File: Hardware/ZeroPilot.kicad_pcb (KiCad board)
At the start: 4 copper layers, 100 x 70 mm, 246 parts, among them J1 Conn_01x03, J10 Conn_01x03, J11 Conn_01x03, J12 Conn_01x03, J13 SPOX-2, J14 Micro_SD_Card, J15 USB_MICRO_B, J16 SPOX-3, J17 SPOX-3, J18 SPOX-4, J19 SPOX-2, J2 Conn_01x03, J22 SPOX-4, J23 SPOX-4, J24 SPOX-6, J25 SPOX-6, J26 SPOX-6, J28 SPOX-6, J29 SPOX-6, J3 Conn_01x03, J30 SPOX-6, J4 Conn_01x03, J5 Conn_01x03, J6 Conn_01x03, J7 Conn_01x03, J8 Conn_01x03, J9 Conn_01x03, Q1 Q_PMOS_DGS, Q2 Q_NMOS_GSD, U1 TPS54308, U10 STM32F030RCT6, U11 M24C64-WDW6TP, U12 ICM-20602, U13 MS5637-02BA03, U14 FT4232H, U2 TPS54308DDCT, U3 NC7S04P5X, U4 TPS22810DRV, U5 TPS22810DRV, U6 TPS22810DRV, U7 TPS22810DRV, U8 MCP1826S-3302E/DB, U9 STM32F765ZGT6, Y1 32.768kHz, Y2 8MHz, Y3 32.768kHz, Y4 8MHz, Y5 Crystal_GND24

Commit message: Changed "Signals" in stackup text to "3.3V"
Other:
- board text added: "Stackup: L1 (Front): Main components and routing L2: Ground L3: 3.3V L4 (Back): USB, SD, more components and routing"
- board text removed: "Stackup: L1 (Front): Main components and routing L2: Ground L3: Signals L4 (Back): USB, SD, more components and routing"
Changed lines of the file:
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@@
     (links 565)
     (no_connects 6)
-    (area 42.734867 94.1 258.863289 174.200001)
+    (area 42.734867 94.1 293.291859 174.200001)
     (thickness 1.6)
     (drawings 5)
@@
       (net 76 /UHF_RX))
   )
-  (gr_text "Stackup:\nL1 (Front): Main components and routing\nL2: Ground\nL3: Signals\nL4 (Back): USB, SD, more components and routing" (at 176.149 120.802) (layer Dwgs.User)
+  (gr_text "Stackup:\nL1 (Front): Main components and routing\nL2: Ground\nL3: 3.3V\nL4 (Back): USB, SD, more components and routing" (at 176.149 120.802) (layer Dwgs.User)
     (effects (font (size 3 3) (thickness 0.3)) (justify left))
   )

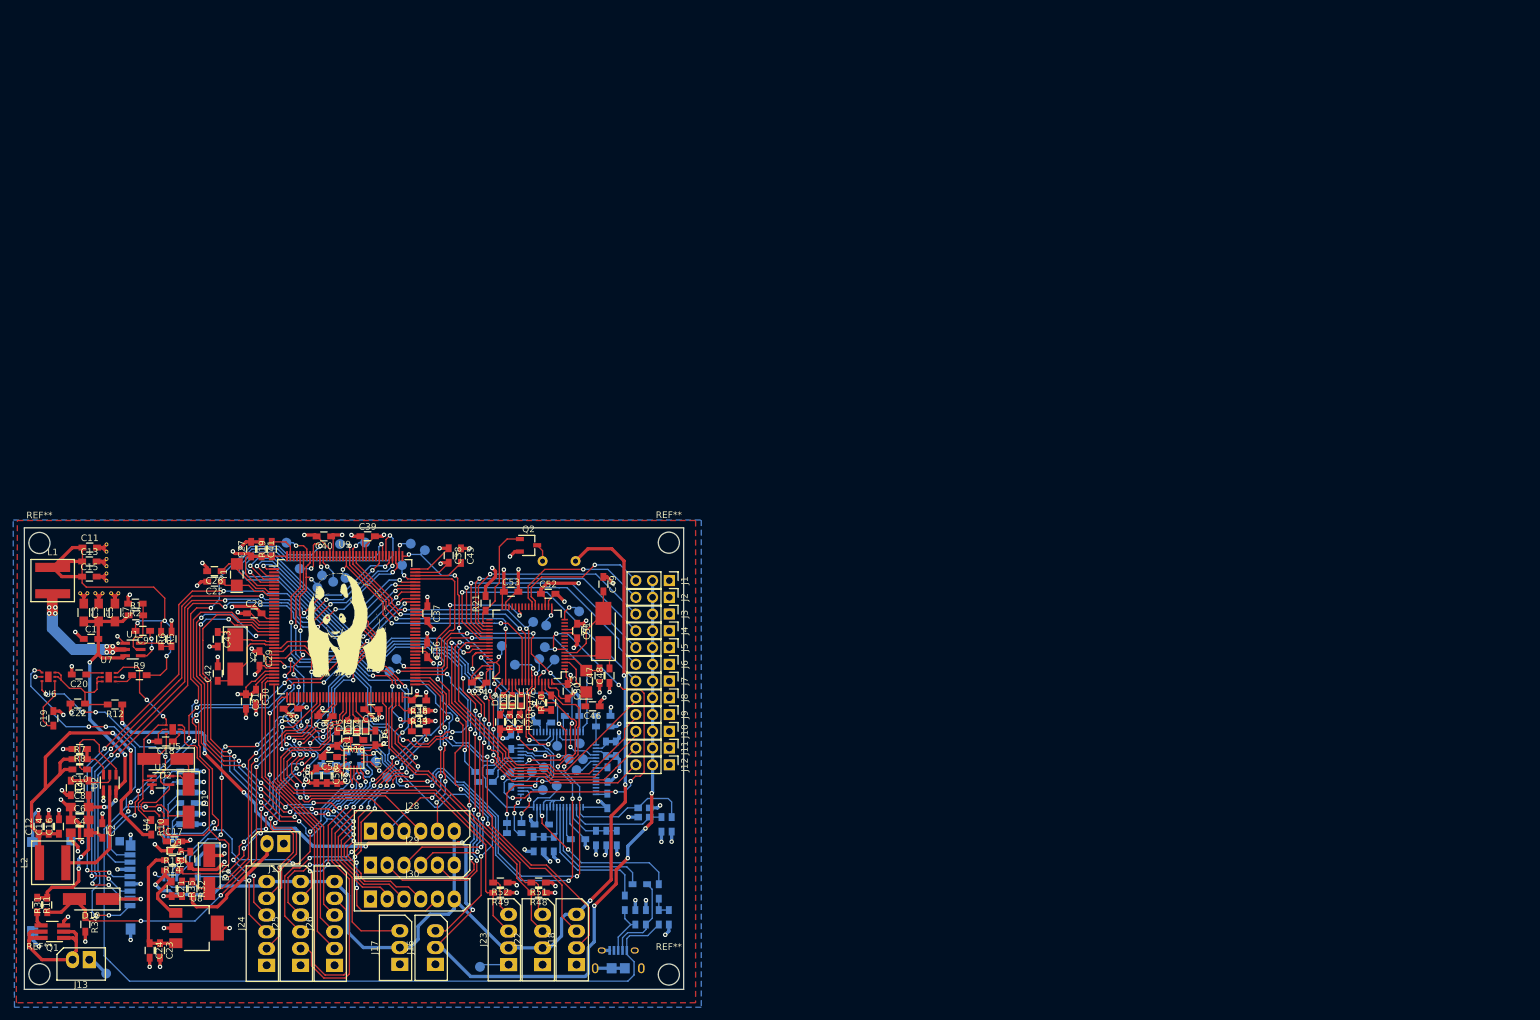
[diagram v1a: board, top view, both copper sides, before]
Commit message: Generated netlist and board outline
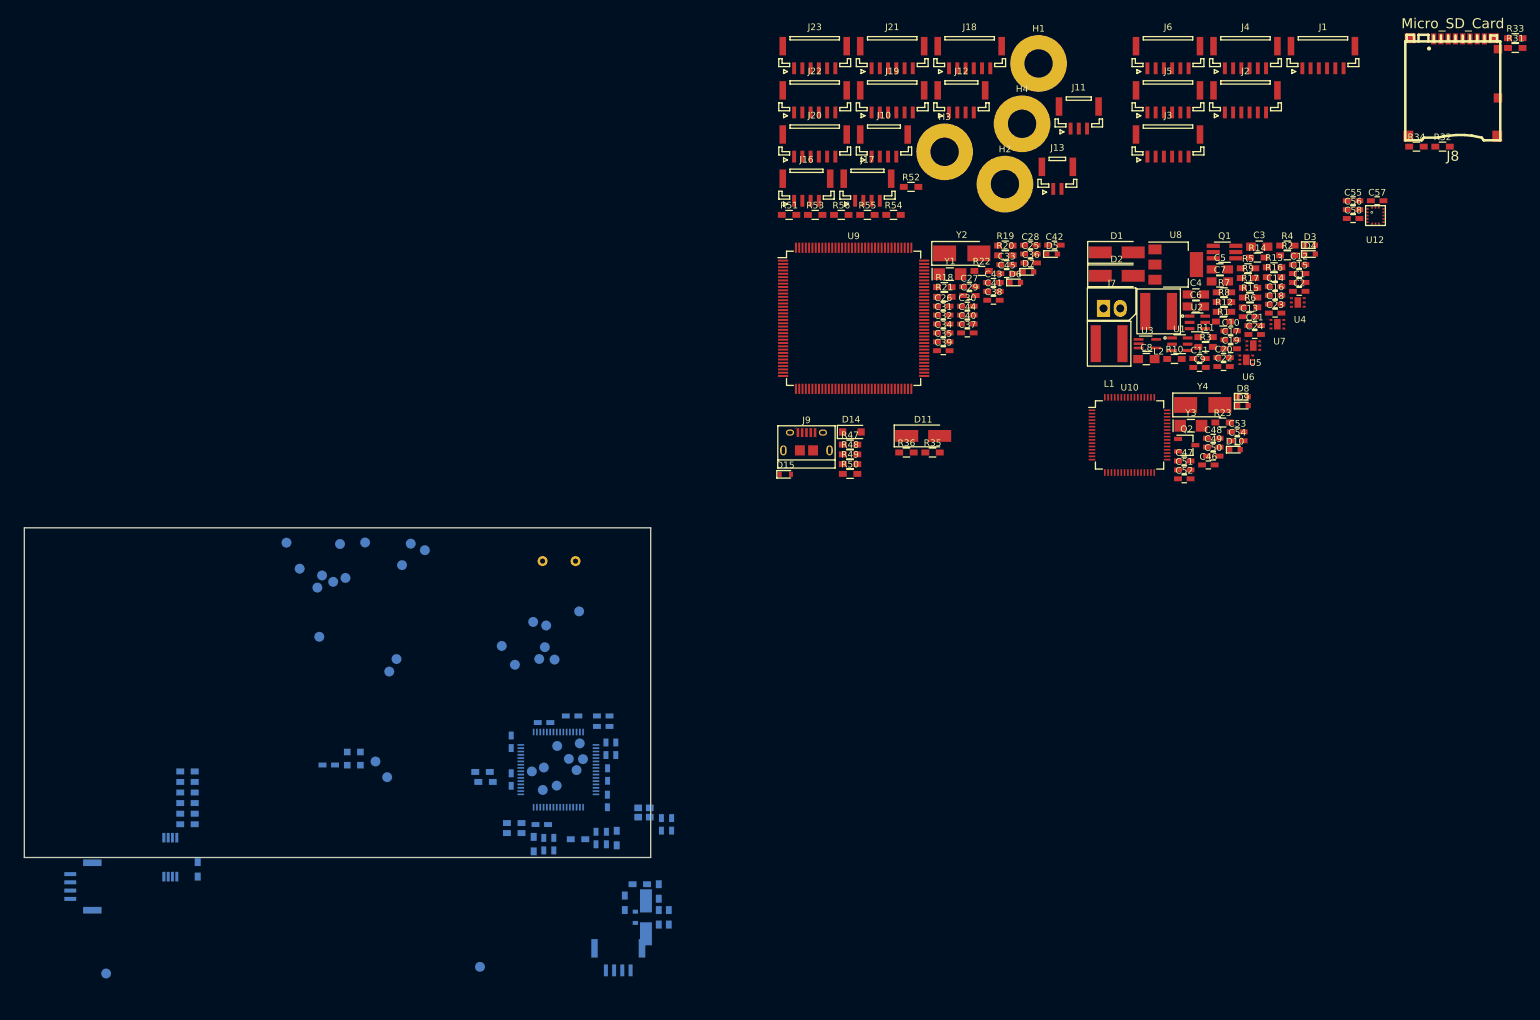
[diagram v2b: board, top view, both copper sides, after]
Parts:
- removed G***: LOGO, WARG:panda_small
- removed J24, J25, J26, J28, J29, J30: SPOX-6, Connectors_Molex:Molex_SPOX-5267_22-03-5065_06x2.54mm_Straight
- removed REF** (x12): via, WARG:via
- removed REF** (x4): MountingHole_3.2mm_M3, Mounting_Holes:MountingHole_3.2mm_M3
- added D14: D_Schottky, Diodes_SMD:D_SOD-123F, F.Cu at (175.5, 85.5)
- added D15: TVS, Diodes_SMD:D_0603, F.Cu at (165.4, 91.9)
- added H1: MountingHole_M4, Mounting_Holes:MountingHole_4.3mm_M4_Pad, F.Cu at (203.8, 29.6)
- added H2: MountingHole_M4, Mounting_Holes:MountingHole_4.3mm_M4_Pad, F.Cu at (198.7, 47.9)
- added H3: MountingHole_M4, Mounting_Holes:MountingHole_4.3mm_M4_Pad, F.Cu at (189.6, 43.0)
- added H4: MountingHole_M4, Mounting_Holes:MountingHole_4.3mm_M4_Pad, F.Cu at (201.3, 38.7)
- added J20: GH-6, Connectors_JST:JST_GH_BM06B-GHS-TBT_06x1.25mm_Straight, F.Cu at (169.9, 42.0)
- added J21: GH-6, Connectors_JST:JST_GH_BM06B-GHS-TBT_06x1.25mm_Straight, F.Cu at (181.6, 28.6)
- added R53: 10K, Resistors_SMD:R_0603_HandSoldering, F.Cu at (169.9, 52.5)
- added R54: 10K, Resistors_SMD:R_0603_HandSoldering, F.Cu at (181.8, 52.5)
- added R55: 10K, Resistors_SMD:R_0603_HandSoldering, F.Cu at (177.9, 52.5)
- added R56: 10K, Resistors_SMD:R_0603_HandSoldering, F.Cu at (173.9, 52.5)
- C1, C10, C11, C12, C13, C14, C15, C16, C17, C18, C19, C2, C20, C21, C22, C23, C24, C25, C26, C27, C28, C29, C30, C31, C32, C33, C34, C35, C36, C37, C38, C39, C40, C41, C42, C43, C44, C45, C46, C47, C48, C49, C50, C51, C52, C53, C54, C55, C57, C59, C60, C61, C62, C63, C64, C65, C66, C67, C68, C69, C70, C71, C72, C73, C74, C75, C76, C9: footprint Resistors_SMD:R_0603_HandSoldering -> Capacitors_SMD:C_0603_HandSoldering
- C3, C4, C5, C6, C7, C8: footprint Resistors_SMD:R_0805_HandSoldering -> Capacitors_SMD:C_0805_HandSoldering
- C56, C58: value 0.1uF -> 100nF; footprint Resistors_SMD:R_0603_HandSoldering -> Capacitors_SMD:C_0603_HandSoldering
- D1, D2: value S1B-13-F -> D
- D10: value D -> LED; footprint Diodes_SMD:D_SMA_Handsoldering -> LEDs:LED_0603
- D12: value TVS -> D; footprint Resistors_SMD:R_0603_HandSoldering -> Diodes_SMD:D_SMA_Handsoldering
- D13: footprint Resistors_SMD:R_0603_HandSoldering -> Diodes_SMD:D_0603
- D4: value LED -> PWR_LED
- J1, J2, J3, J4, J5, J6: value Conn_01x03 -> GH-6; footprint Pin_Headers:Pin_Header_Straight_1x03_Pitch2.54mm -> Connectors_JST:JST_GH_BM06B-GHS-TBT_06x1.25mm_Straight
- J10, J12: value Conn_01x03 -> GH-4; footprint Pin_Headers:Pin_Header_Straight_1x03_Pitch2.54mm -> Connectors_JST:JST_GH_BM04B-GHS-TBT_04x1.25mm_Straight
- J11: value Conn_01x03 -> GH-3; footprint Pin_Headers:Pin_Header_Straight_1x03_Pitch2.54mm -> Connectors_JST:JST_GH_BM03B-GHS-TBT_03x1.25mm_Straight
- J13: value SPOX-2 -> GH-2; footprint Connectors_Molex:Molex_SPOX-5267_22-03-5025_02x2.54mm_Straight -> Connectors_JST:JST_GH_BM02B-GHS-TBT_02x1.25mm_Straight
- J14: value Micro_SD_Card -> GH-4; footprint WARG:micro_sd -> Connectors_JST:JST_GH_BM04B-GHS-TBT_04x1.25mm_Straight
- J15: value USB_MICRO_B -> GH-4; footprint WARG:USB_Micro-B_10118194-0001LF -> Connectors_JST:JST_GH_BM04B-GHS-TBT_04x1.25mm_Straight
- J16, J17: value SPOX-3 -> GH-4; footprint Connectors_Molex:Molex_SPOX-5267_22-03-5035_03x2.54mm_Straight -> Connectors_JST:JST_GH_BM04B-GHS-TBT_04x1.25mm_Straight
- J18, J22, J23: value SPOX-4 -> GH-6; footprint Connectors_Molex:Molex_SPOX-5267_22-03-5045_04x2.54mm_Straight -> Connectors_JST:JST_GH_BM06B-GHS-TBT_06x1.25mm_Straight
- J19: value SPOX-2 -> GH-6; footprint Connectors_Molex:Molex_SPOX-5267_22-03-5025_02x2.54mm_Straight -> Connectors_JST:JST_GH_BM06B-GHS-TBT_06x1.25mm_Straight
- J7: value Conn_01x03 -> SPOX-2; footprint Pin_Headers:Pin_Header_Straight_1x03_Pitch2.54mm -> Connectors_Molex:Molex_SPOX-5267_22-03-5025_02x2.54mm_Straight
- J8: value Conn_01x03 -> Micro_SD_Card; footprint Pin_Headers:Pin_Header_Straight_1x03_Pitch2.54mm -> WARG:micro_sd
- J9: value Conn_01x03 -> USB_MICRO_B; footprint Pin_Headers:Pin_Header_Straight_1x03_Pitch2.54mm -> WARG:USB_Micro-B_10118194-0001LF
- L3, L4: footprint Resistors_SMD:R_0603_HandSoldering -> Inductors_SMD:L_0603_HandSoldering
- R1: value 210k -> 210K
- R19, R26: value 0 -> 100
- R2: value 43.2k -> 43.2K
- R21: value 100K -> 10K
- R22: value 100 -> 0
- R24: value 0 -> 100K
- R25: value 10K -> 100
- R3: value 226k -> 226K
- R30, R48, R49: value 10K -> 0
- R31: value 150K -> 10K
- R32: value 150K -> 0
- R33: value 11K -> 10K
- R34: value 22K -> 10K
- R35, R36: value 22K -> 150K
- R37: value 4.7k -> 11K
- R38: value 10k -> 22K
- R39: value 12k -> 22K
- R4: value 56k -> 56K
- R40: value 10R -> 22K
- R41: value 10R -> 4.7K
- R42: value 1k -> 10K
- R43: value 220R -> 12K
- R44, R45: value 0R -> 10
- R46: value 220R -> 1K
- R47, R50: value 10K -> 220
- R5, R7: value 100k -> 100K
- R6: value 11k -> 11K
- R8: value 13.7k -> 13.7K
- TP10: value NRSTS_TST -> GND_TST
- TP11: value SWIOS_TST -> TXP_TST
- TP12: value SCLKS_TST -> RXP_TST
- TP13: value NRSTP_TST -> NRSTS_TST
- TP14: value SWIOP_TST -> SWIOS_TST
- TP15: value SCLKP_TST -> SCLKS_TST
- TP16: value GND_TST -> NRSTP_TST
- TP17: value TDO1_TST -> SWIOP_TST
- TP18: value TMS1_TST -> SCLKP_TST
- TP19: value TEST -> GND_TST
- TP20: value TDO2_TST -> TDO1_TST
- TP21: value TMS2_TST -> TMS1_TST
- TP22: value TEST -> TDO2_TST
- TP23: value UART1_RTS_TST -> TMS2_TST
- TP24: value UART1_CTS_TST -> UART1_RTS_TST
- TP25: value UART2_RTS_TST -> UART1_CTS_TST
- TP26: value UART2_CTS_TST -> UART2_RTS_TST
- TP27: value TEST -> UART2_CTS_TST
- TP5: value TXS_TST -> TEST
- TP6: value RXS_TST -> TEST
- TP7: value GND_TST -> TEST
- TP8: value TXP_TST -> TXS_TST
- TP9: value RXP_TST -> RXS_TST
- moved R31 257.8 mm to (276.1, 27.2), turned to 0 degrees
- moved R34 233.8 mm to (261.1, 42.2), turned to 0 degrees
- moved R32 220.5 mm to (265.1, 42.2), turned to 0 degrees
- moved C12 209.3 mm to (243.3, 60.1), turned to 0 degrees
- moved Q1 205.5 mm to (232.0, 58.2), turned to 0 degrees
- moved C14 203.2 mm to (239.7, 63.4), turned to 0 degrees
- moved R4 202.0 mm to (241.6, 57.2), turned to 0 degrees
- moved C16 201.3 mm to (239.7, 64.7), turned to 0 degrees
- moved C2 199.1 mm to (243.4, 64.1), turned to 0 degrees
- moved R11 197.0 mm to (229.2, 71.1), turned to 0 degrees
- moved R33 196.7 mm to (276.1, 25.7)
- moved D3 195.0 mm to (245.0, 57.1)
- moved C23 194.8 mm to (239.7, 67.4), turned to 0 degrees
- moved C24 191.9 mm to (236.6, 70.7), turned to 0 degrees
- moved C1 191.0 mm to (243.4, 62.8)
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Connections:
- C10 pad 2: /POWER/INT_BUCK -> /POWER/INT_SW
- C9 pad 2: /POWER/EXT_BUCK -> /POWER/EXT_SW
- D10 pad 1: /3V3 -> Net-(D10-Pad1)
- D10 pad 2: /VBATT_ADC -> Net-(D10-Pad2)
- D11 pad 2: /EXT_BATT_ADC -> /VBATT_ADC
- D12 pad 1: Net-(D12-Pad1) -> /3V3
- D12 pad 2: GND -> /V_ISENSE_ADC
- D4 pad 1: Net-(D4-Pad1) -> GND
- J1 pad 1: GND -> /6V_EXT
- J10 pad 2: /6V_EXT -> /RSSI
- J10 pad 3: /PWM 1-12/PWM10 -> /PPM
- J11 pad 2: /6V_EXT -> /5V_INT
- J11 pad 3: /PWM 1-12/PWM11 -> /AIR_SPD
- J12 pad 2: /6V_EXT -> /ULTRA_SONIC_1
- J12 pad 3: /PWM 1-12/PWM12 -> /ULTRA_SONIC_2
- J13 pad 2: /POWER/BATT_IN -> /V_ISENSE
- J14 pad 1: /SD_D2 -> GND
- J14 pad 2: /SD_D3 -> /UHF_RX
- J14 pad 3: /SD_CMD -> /UHF_TX
- J14 pad 4: /3V3 -> /6V_EXT
- J15 pad 1: /5V_USB -> GND
- J15 pad 2: Net-(D12-Pad1) -> /SCL4
- J15 pad 3: Net-(D13-Pad1) -> /SDA4
- J15 pad 4: Net-(J15-Pad4) -> /5V_INT
- J16 pad 2: /6V_EXT -> /SCL4
- J16 pad 3: /PPM -> /SDA4
- J17 pad 2: /5V_INT -> /SCL4
- J17 pad 3: /AIR_SPD -> /SDA4
- J18 pad 2: /ULTRA_SONIC_1 -> /RTS1
- J18 pad 3: /ULTRA_SONIC_2 -> /TX1
- J18 pad 4: /5V_INT -> /RX1
- J19 pad 2: /EXT_BATT -> /RTS4
- J2 pad 1: GND -> /6V_EXT
- J2 pad 3: /PWM 1-12/PWM2 -> /PWM 1-12/PWM3
- J22 pad 2: /5V_INT -> /NSS4
- J22 pad 3: /SCL2 -> /MOSI4
- J22 pad 4: /SDA2 -> /MISO4
- J23 pad 2: /5V_INT -> /NSS5
- J23 pad 3: /SCL4 -> /MOSI5
- J23 pad 4: /SDA4 -> /MISO5
- J3 pad 1: GND -> /6V_EXT
- J3 pad 3: /PWM 1-12/PWM3 -> /PWM 1-12/PWM5
- J4 pad 1: GND -> /6V_EXT
- J4 pad 3: /PWM 1-12/PWM4 -> /PWM 1-12/PWM7
- J5 pad 1: GND -> /6V_EXT
- J5 pad 3: /PWM 1-12/PWM5 -> /PWM 1-12/PWM9
- J6 pad 1: GND -> /6V_EXT
- J6 pad 3: /PWM 1-12/PWM6 -> /PWM 1-12/PWM11
- J7 pad 2: /6V_EXT -> /POWER/BATT_IN
- J8 pad 1: GND -> /SD_D2
- J8 pad 2: /6V_EXT -> /SD_D3
- J8 pad 3: /PWM 1-12/PWM8 -> /SD_CMD
- J9 pad 1: GND -> Net-(D14-Pad2)
- J9 pad 2: /6V_EXT -> Net-(D13-Pad1)
- J9 pad 3: /PWM 1-12/PWM9 -> Net-(D15-Pad1)
- R16 pad 1: Net-(D4-Pad1) -> /6V_EXT
- R16 pad 2: GND -> Net-(R16-Pad2)
- R17 pad 1: Net-(D5-Pad1) -> Net-(R16-Pad2)
- R17 pad 2: GND -> Net-(D4-Pad2)
- R18 pad 1: Net-(D6-Pad1) -> Net-(D5-Pad1)
- R19 pad 1: /3V3 -> Net-(D6-Pad1)
- R19 pad 2: Net-(R19-Pad2) -> GND
- R21 pad 1: Net-(Q2-Pad1) -> GND
- R21 pad 2: GND -> Net-(R21-Pad2)
- R22 pad 1: Net-(D8-Pad1) -> /3V3
- R22 pad 2: GND -> Net-(R22-Pad2)
- R23 pad 1: Net-(D9-Pad1) -> Net-(D8-Pad1)
- R24 pad 1: /3V3 -> Net-(Q2-Pad1)
- R24 pad 2: /MEMORY/E1 -> GND
- R25 pad 1: /MEMORY/E1 -> Net-(D9-Pad1)
- R26 pad 1: /3V3 -> Net-(D10-Pad1)
- R26 pad 2: /MEMORY/E2 -> GND
- R27 pad 1: /MEMORY/E2 -> Net-(R27-Pad1)
- R28 pad 2: /MEMORY/E3 -> /MEMORY/E1
- R29 pad 1: /MEMORY/E3 -> /MEMORY/E1
- R30 pad 2: /MEM_WC -> /MEMORY/E2
- R31 pad 1: /VBATT_ADC -> /MEMORY/E2
- R31 pad 2: /VBATT -> GND
- R32 pad 1: /EXT_BATT_ADC -> /3V3
- R32 pad 2: /EXT_BATT -> /MEMORY/E3
- R33 pad 1: /AIRSPD_ADC -> /MEMORY/E3
- R33 pad 2: /AIR_SPD -> GND
- R34 pad 1: /VBATT_ADC -> /3V3
- R34 pad 2: GND -> /MEM_WC
- R35 pad 1: /EXT_BATT_ADC -> /VBATT_ADC
- R35 pad 2: GND -> /VBATT
- R36 pad 1: /AIRSPD_ADC -> /V_ISENSE_ADC
- R36 pad 2: GND -> /V_ISENSE
- R37 pad 1: /5V_USB -> /AIRSPD_ADC
- R37 pad 2: Net-(R37-Pad2) -> /AIR_SPD
- R38 pad 1: Net-(R37-Pad2) -> /VBATT_ADC
- R39 pad 1: Net-(R39-Pad1) -> /V_ISENSE_ADC
- R40 pad 1: Net-(R40-Pad1) -> /AIRSPD_ADC
- R40 pad 2: Net-(D13-Pad1) -> GND
- R41 pad 1: Net-(R41-Pad1) -> /5V_USB
- R41 pad 2: Net-(D12-Pad1) -> Net-(R41-Pad2)
- R42 pad 1: Net-(R42-Pad1) -> Net-(R41-Pad2)
- R42 pad 2: Net-(R37-Pad2) -> GND
- R43 pad 2: /SWIO_SAFETY -> GND
- R44 pad 2: /SWIO_SAFETY -> Net-(D15-Pad1)
- R45 pad 2: /SWIO_PILOT -> Net-(D13-Pad1)
- R46 pad 2: /SWIO_PILOT -> Net-(R41-Pad2)
- R47 pad 1: /3V3 -> Net-(R47-Pad1)
- R47 pad 2: /SCL1 -> /SWIO_SAFETY
- R48 pad 1: /3V3 -> Net-(R48-Pad1)
- R48 pad 2: /SCL2 -> /SWIO_SAFETY
- R49 pad 1: /3V3 -> Net-(R49-Pad1)
- R49 pad 2: /SCL4 -> /SWIO_PILOT
- R50 pad 1: /3V3 -> Net-(R50-Pad1)
- R50 pad 2: /SDA1 -> /SWIO_PILOT
- R51 pad 2: /SDA2 -> /SCL1
- R52 pad 2: /SDA4 -> /SCL2
- TP10 pad 1: /NRST_SAFETY -> GND
- TP11 pad 1: /SWIO_SAFETY -> /TX3
- TP12 pad 1: /SCLK_SAFETY -> /RX3
- TP13 pad 1: /NRST_PILOT -> /NRST_SAFETY
- TP14 pad 1: /SWIO_PILOT -> /SWIO_SAFETY
- TP15 pad 1: /SCLK_PILOT -> /SCLK_SAFETY
- TP16 pad 1: GND -> /NRST_PILOT
- TP17 pad 1: /TDO1_TST -> /SWIO_PILOT
- TP18 pad 1: /TMS1_TST -> /SCLK_PILOT
- TP19 pad 1: /UHF_TX -> GND
- TP20 pad 1: /TDO2_TST -> /TDO1_TST
- TP21 pad 1: /TMS2_TST -> /TMS1_TST
- TP22 pad 1: /UHF_RX -> /TDO2_TST
- TP23 pad 1: /UART1_RTS_TST -> /TMS2_TST
- TP24 pad 1: /UART1_CTS_TST -> /UART1_RTS_TST
- TP25 pad 1: /UART2_RTS_TST -> /UART1_CTS_TST
- TP26 pad 1: /UART2_CTS_TST -> /UART2_RTS_TST
- TP27 pad 1: /TDI -> /UART2_CTS_TST
- TP28 pad 1: /TDO -> /SDA1
- TP29 pad 1: /JRST -> /SCL1
- TP3 pad 1: Net-(TP3-Pad1) -> /TDI
- TP30 pad 1: /SDA1 -> /SDA2
- TP31 pad 1: /SCL1 -> /SCL2
- TP4 pad 1: Net-(TP4-Pad1) -> /TDO
- TP5 pad 1: /SAFETY_DBG_TX -> /JRST
- TP6 pad 1: /SAFETY_DBG_RX -> Net-(R21-Pad2)
- TP7 pad 1: GND -> Net-(R27-Pad1)
- TP8 pad 1: /TX3 -> /SAFETY_DBG_TX
- TP9 pad 1: /RX3 -> /SAFETY_DBG_RX
- U10 pad 10: Net-(U10-Pad10) -> (no net)
- U10 pad 11: Net-(U10-Pad11) -> (no net)
- U10 pad 14: Net-(U10-Pad14) -> (no net)
- U10 pad 15: Net-(U10-Pad15) -> (no net)
- U10 pad 2: Net-(U10-Pad2) -> (no net)
- U10 pad 20: Net-(U10-Pad20) -> (no net)
- U10 pad 21: Net-(U10-Pad21) -> (no net)
- U10 pad 24: Net-(U10-Pad24) -> (no net)
- U10 pad 25: Net-(U10-Pad25) -> (no net)
- U10 pad 26: Net-(U10-Pad26) -> /RSSI
- U10 pad 28: Net-(U10-Pad28) -> (no net)
- U10 pad 29: Net-(U10-Pad29) -> (no net)
- U10 pad 30: Net-(U10-Pad30) -> (no net)
- U10 pad 33: Net-(U10-Pad33) -> (no net)
- U10 pad 45: Net-(U10-Pad45) -> (no net)
- U10 pad 50: /NSS1 -> (no net)
- U10 pad 51: Net-(D9-Pad2) -> Net-(D10-Pad2)
- U10 pad 52: Net-(D8-Pad2) -> Net-(D9-Pad2)
- U10 pad 53: Net-(D7-Pad2) -> Net-(D8-Pad2)
- U10 pad 54: Net-(U10-Pad54) -> (no net)
- U10 pad 55: /SCK1 -> (no net)
- U10 pad 56: /MISO1 -> (no net)
- U10 pad 57: /MOSI1 -> (no net)
- U10 pad 58: /SAFETY_DBG_RX -> /SAFETY_DBG_TX
- U10 pad 59: /SAFETY_DBG_TX -> /SAFETY_DBG_RX
- U10 pad 60: Net-(TP4-Pad1) -> Net-(R27-Pad1)
- U10 pad 8: Net-(U10-Pad8) -> (no net)
- U10 pad 9: Net-(U10-Pad9) -> (no net)
- U12 pad 15: Net-(U12-Pad15) -> GND
- U12 pad 2: /SCK5 -> /SCK1
- U12 pad 3: /MOSI5 -> /MOSI1
- U12 pad 4: /MISO5 -> /MISO1
- U12 pad 5: /NSS5 -> /NSS1
- U12 pad 7: Net-(U12-Pad7) -> (no net)
- U13 pad 2: /SDA1 -> /SDA2
- U13 pad 3: /SCL1 -> /SCL2
- U14 pad 14: Net-(R42-Pad1) -> Net-(R46-Pad1)
- U14 pad 17: Net-(R43-Pad1) -> Net-(R47-Pad1)
- U14 pad 18: Net-(R44-Pad1) -> Net-(R48-Pad1)
- U14 pad 23: Net-(U14-Pad23) -> (no net)
- U14 pad 24: Net-(U14-Pad24) -> (no net)
- U14 pad 27: Net-(R46-Pad1) -> Net-(R50-Pad1)
- U14 pad 28: Net-(R45-Pad1) -> Net-(R49-Pad1)
- U14 pad 33: Net-(U14-Pad33) -> (no net)
- U14 pad 34: Net-(U14-Pad34) -> (no net)
- U14 pad 36: Net-(U14-Pad36) -> (no net)
- U14 pad 43: Net-(U14-Pad43) -> (no net)
- U14 pad 44: Net-(U14-Pad44) -> (no net)
- U14 pad 45: Net-(U14-Pad45) -> (no net)
- U14 pad 46: Net-(U14-Pad46) -> (no net)
- U14 pad 55: Net-(U14-Pad55) -> (no net)
- U14 pad 57: Net-(U14-Pad57) -> (no net)
- U14 pad 58: Net-(U14-Pad58) -> (no net)
- U14 pad 59: Net-(U14-Pad59) -> (no net)
- U14 pad 6: Net-(R39-Pad1) -> Net-(R43-Pad1)
- U14 pad 60: Net-(U14-Pad60) -> (no net)
- U14 pad 61: Net-(U14-Pad61) -> (no net)
- U14 pad 62: Net-(U14-Pad62) -> (no net)
- U14 pad 63: Net-(U14-Pad63) -> (no net)
- U14 pad 7: Net-(R41-Pad1) -> Net-(R45-Pad1)
- U14 pad 8: Net-(R40-Pad1) -> Net-(R44-Pad1)
- U3 pad 1: Net-(U3-Pad1) -> (no net)
- U9 pad 10: Net-(U9-Pad10) -> (no net)
- U9 pad 100: Net-(U9-Pad100) -> (no net)
- U9 pad 11: Net-(U9-Pad11) -> (no net)
- U9 pad 114: /TX4 -> /RX4
- U9 pad 115: /RX4 -> /TX4
- U9 pad 117: Net-(U9-Pad117) -> (no net)
- U9 pad 118: Net-(U9-Pad118) -> (no net)
- U9 pad 119: Net-(U9-Pad119) -> (no net)
- U9 pad 12: Net-(U9-Pad12) -> (no net)
- U9 pad 122: Net-(U9-Pad122) -> (no net)
- U9 pad 127: Net-(U9-Pad127) -> (no net)
- U9 pad 128: Net-(U9-Pad128) -> (no net)
- U9 pad 129: Net-(U9-Pad129) -> (no net)
- U9 pad 13: Net-(U9-Pad13) -> (no net)
- U9 pad 132: Net-(U9-Pad132) -> (no net)
- U9 pad 135: Net-(U9-Pad135) -> (no net)
- U9 pad 138: Net-(TP3-Pad1) -> Net-(R21-Pad2)
- U9 pad 14: Net-(U9-Pad14) -> (no net)
- U9 pad 141: Net-(U9-Pad141) -> (no net)
- U9 pad 142: Net-(U9-Pad142) -> (no net)
- U9 pad 143: Net-(R19-Pad2) -> Net-(R22-Pad2)
- U9 pad 15: Net-(U9-Pad15) -> (no net)
- U9 pad 2: Net-(U9-Pad2) -> (no net)
- U9 pad 22: Net-(U9-Pad22) -> (no net)
- U9 pad 27: Net-(U9-Pad27) -> (no net)
- U9 pad 40: Net-(U9-Pad40) -> (no net)
- U9 pad 41: Net-(U9-Pad41) -> (no net)
- U9 pad 42: Net-(U9-Pad42) -> (no net)
- U9 pad 43: Net-(U9-Pad43) -> (no net)
- U9 pad 44: Net-(U9-Pad44) -> (no net)
- U9 pad 45: Net-(U9-Pad45) -> (no net)
- U9 pad 46: /EXT_BATT_ADC -> /V_ISENSE_ADC
- U9 pad 48: Net-(U9-Pad48) -> (no net)
- U9 pad 49: Net-(U9-Pad49) -> (no net)
- U9 pad 50: Net-(U9-Pad50) -> (no net)
- U9 pad 53: Net-(U9-Pad53) -> (no net)
- U9 pad 56: Net-(D5-Pad2) -> Net-(D6-Pad2)
- U9 pad 57: Net-(D6-Pad2) -> Net-(D7-Pad2)
- U9 pad 58: Net-(D4-Pad2) -> Net-(D5-Pad2)
- U9 pad 59: Net-(U9-Pad59) -> (no net)
- U9 pad 60: Net-(U9-Pad60) -> (no net)
- U9 pad 63: Net-(U9-Pad63) -> (no net)
- U9 pad 64: Net-(U9-Pad64) -> (no net)
- U9 pad 65: Net-(U9-Pad65) -> (no net)
- U9 pad 67: Net-(U9-Pad67) -> (no net)
- U9 pad 68: Net-(U9-Pad68) -> (no net)
- U9 pad 7: Net-(U9-Pad7) -> (no net)
- U9 pad 79: Net-(U9-Pad79) -> (no net)
- U9 pad 80: Net-(U9-Pad80) -> (no net)
- U9 pad 81: Net-(U9-Pad81) -> (no net)
- U9 pad 82: Net-(U9-Pad82) -> (no net)
- U9 pad 85: Net-(U9-Pad85) -> (no net)
- U9 pad 86: Net-(U9-Pad86) -> (no net)
- U9 pad 87: Net-(U9-Pad87) -> (no net)
- U9 pad 88: Net-(U9-Pad88) -> (no net)
- U9 pad 89: Net-(U9-Pad89) -> (no net)
- U9 pad 90: Net-(U9-Pad90) -> (no net)
- U9 pad 91: Net-(U9-Pad91) -> (no net)
- U9 pad 92: Net-(U9-Pad92) -> (no net)
- U9 pad 93: Net-(U9-Pad93) -> (no net)
- U9 pad 96: Net-(U9-Pad96) -> (no net)
- U9 pad 97: Net-(U9-Pad97) -> (no net)
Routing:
- net GND: track 327.5 -> 0.28 mm, vias 98 -> 0
- net /SCL1: track 203.4 -> 0.00 mm, vias 13 -> 0
- net /3V3: track 177.3 -> 0.00 mm, vias 37 -> 0
- net /6V_EXT: track 172.2 -> 0.00 mm, vias 10 -> 0
- net /5V_INT: track 171.9 -> 0.00 mm, vias 4 -> 0
- net /5V_USB: track 162.3 -> 0.00 mm, vias 4 -> 0
- net /SDA1: track 161.8 -> 0.00 mm, vias 14 -> 0
- net /TX4: track 118.6 -> 0.00 mm, vias 10 -> 0
- net /RX4: track 111.4 -> 0.00 mm, vias 10 -> 0
- net /SD_D2: track 98.8 -> 0.00 mm, vias 7 -> 0
- net /SCK5: track 97.3 -> 0.00 mm, vias 7 -> 0
- net /SD_D3: track 93.4 -> 0.00 mm, vias 7 -> 0
- net /ULTRA_SONIC_1: track 92.5 -> 0.00 mm, vias 4 -> 0
- net /SD_CK: track 91.5 -> 0.00 mm, vias 7 -> 0
- net /SD_CMD: track 90.2 -> 0.00 mm, vias 7 -> 0
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- removed copper zone on B.Cu, net GND
- removed copper zone on F.Cu, net GND
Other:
- board size 100 x 70 mm -> 95 x 50 mm

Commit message: Initial Routing of Zeropilot Rev1
This is the initial routing of the board. It needs to be cleaned up slightly, but library references are screwed up so they will be fixed first.
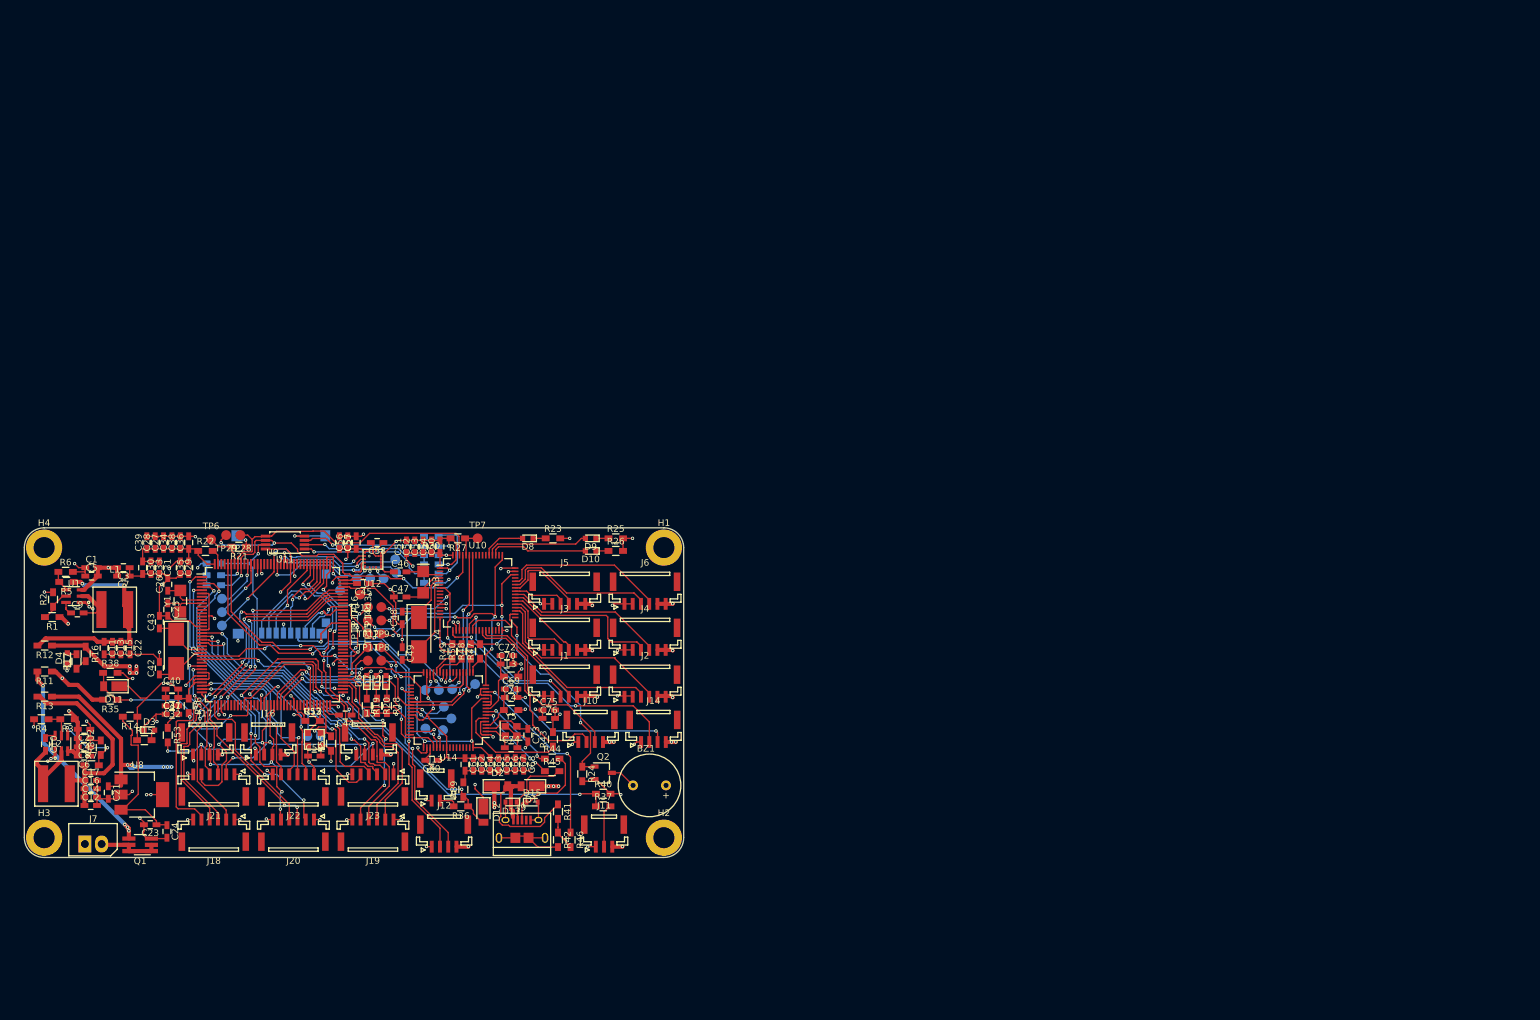
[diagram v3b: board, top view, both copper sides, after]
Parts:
- removed C18, C19, C20: 10nF, Capacitors_SMD:C_0603_HandSoldering
- removed D14: D_Schottky, Diodes_SMD:D_SOD-123F
- removed R10, R9: 0, Resistors_SMD:R_0603_HandSoldering
- removed TP10: GND_TST, Measurement_Points:Measurement_Point_Round-SMD-Pad_Small
- removed U3: NC7S04P5X, TO_SOT_Packages_SMD:SOT-353_SC-70-5_Handsoldering
- removed U4, U5, U6, U7: TPS22810DRV, WARG:TPS22810DRV
- BZ1, C59, C60, C61, C62, C63, C64, C65, C66, C67, C68, C69, C70, C71, C72, C73, C74, C75, C76, D13, J14, J15, L3, L4, R24, R25, R26, R27, R37, R38, R39, R40, R41, R42, R43, R44, R45, R46, TP11, TP12, TP13, TP14, TP15, TP16, TP17, TP18, TP19, TP28, TP29, TP6, TP7, TP8, TP9, U11, U13, U14, Y5: moved to F.Cu
- C17: value 10nF -> 1uF
- C3, C4, C5, C6, C7, C8: footprint Capacitors_SMD:C_0805_HandSoldering -> Capacitors_SMD:C_0603_HandSoldering
- D1, D11, D2: footprint Diodes_SMD:D_SMA_Handsoldering -> Diodes_SMD:D_PowerDI-123
- D12: footprint Diodes_SMD:D_SMA_Handsoldering -> Diodes_SMD:D_PowerDI-123; moved to F.Cu
- H1, H2, H3, H4: value MountingHole_M4 -> MountingHole_M3; footprint Mounting_Holes:MountingHole_4.3mm_M4_Pad -> Mounting_Holes:MountingHole_3.2mm_M3_ISO14580_Pad
- J8, R31, R32, R33, R34, R51, R54: moved to B.Cu
- moved R4 202.2 mm to (52.6, 129.0), turned to 180 degrees
- moved C12 200.8 mm to (60.1, 142.1)
- moved D4 198.2 mm to (56.5, 119.8), turned to 90 degrees
- moved R13 197.5 mm to (53.1, 125.6), turned to 180 degrees
- moved C2 195.9 mm to (59.1, 130.6), turned to 180 degrees
- moved C14 195.6 mm to (60.1, 140.8)
- moved C16 194.6 mm to (60.1, 139.6)
- moved R2 194.3 mm to (54.4, 110.9), turned to 90 degrees
- moved J8 193.1 mm to (88.9, 108.6)
- moved R34 193.0 mm to (78.7, 105.4)
- moved D3 190.8 mm to (69.0, 130.7)
- moved C10 190.4 mm to (53.2, 132.8), turned to 270 degrees
- moved R16 189.1 mm to (59.3, 119.1), turned to 270 degrees
- moved C1 188.2 mm to (60.2, 106.0)
- moved C21 187.7 mm to (62.7, 140.1), turned to 270 degrees
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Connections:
- C11 pad 1: /POWER/EXT_BUCK -> /POWER/6V_EXT_JMP
- C12 pad 1: /POWER/INT_BUCK -> /POWER/5V_INT_JMP
- C13 pad 1: /POWER/EXT_BUCK -> /POWER/6V_EXT_JMP
- C14 pad 1: /POWER/INT_BUCK -> /POWER/5V_INT_JMP
- C15 pad 1: /POWER/EXT_BUCK -> /POWER/6V_EXT_JMP
- C16 pad 1: /POWER/INT_BUCK -> /POWER/5V_INT_JMP
- C17 pad 1: Net-(C17-Pad1) -> /POWER/5V_INT_JMP
- D1 pad 1: Net-(D1-Pad1) -> /6V_EXT
- D2 pad 1: Net-(D1-Pad1) -> /5V_INT
- D2 pad 2: /POWER/INT_JMP1 -> /5V_USB
- J1 pad 1: /6V_EXT -> GND
- J1 pad 2: /6V_EXT -> GND
- J1 pad 5: GND -> /6V_EXT
- J1 pad 6: GND -> /6V_EXT
- J11 pad 2: /5V_INT -> /AIR_SPD
- J11 pad 3: /AIR_SPD -> /5V_INT
- J2 pad 1: /6V_EXT -> GND
- J2 pad 2: /6V_EXT -> GND
- J2 pad 5: GND -> /6V_EXT
- J2 pad 6: GND -> /6V_EXT
- J3 pad 1: /6V_EXT -> GND
- J3 pad 2: /6V_EXT -> GND
- J3 pad 5: GND -> /6V_EXT
- J3 pad 6: GND -> /6V_EXT
- J4 pad 1: /6V_EXT -> GND
- J4 pad 2: /6V_EXT -> GND
- J4 pad 5: GND -> /6V_EXT
- J4 pad 6: GND -> /6V_EXT
- J5 pad 1: /6V_EXT -> GND
- J5 pad 2: /6V_EXT -> GND
- J5 pad 5: GND -> /6V_EXT
- J5 pad 6: GND -> /6V_EXT
- J6 pad 1: /6V_EXT -> GND
- J6 pad 2: /6V_EXT -> GND
- J6 pad 5: GND -> /6V_EXT
- J6 pad 6: GND -> /6V_EXT
- J9 pad 1: Net-(D14-Pad2) -> /5V_USB
- L1 pad 1: /POWER/EXT_BUCK -> /POWER/6V_EXT_JMP
- L2 pad 1: /POWER/INT_BUCK -> /POWER/5V_INT_JMP
- R5 pad 1: /POWER/EXT_BUCK -> /POWER/6V_EXT_JMP
- R7 pad 1: /POWER/INT_BUCK -> /POWER/5V_INT_JMP
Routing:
- net GND: track 0.28 -> 309.8 mm, vias 0 -> 77
- net /3V3: track 0.00 -> 177.4 mm, vias 0 -> 28
- net /AIRSPD_ADC: track 0.00 -> 70.3 mm, vias 0 -> 2
- net /ULTRA_SONIC_2: track 0.00 -> 69.3 mm, vias 0 -> 2
- net /ULTRA_SONIC_1: track 0.00 -> 67.7 mm, vias 0 -> 2
- net /SCL1: track 0.00 -> 59.6 mm, vias 0 -> 5
- net /CTS1: track 0.00 -> 57.8 mm, vias 0 -> 4
- net /RX1: track 0.00 -> 53.6 mm, vias 0 -> 4
- net /TX1: track 0.00 -> 52.6 mm, vias 0 -> 4
- net /V_ISENSE_ADC: track 0.00 -> 52.5 mm, vias 0 -> 2
- net /RTS1: track 0.00 -> 52.3 mm, vias 0 -> 4
- net /TX4: track 0.00 -> 50.3 mm, vias 0 -> 4
- net /5V_INT: track 0.00 -> 49.5 mm, vias 0 -> 18
- net /RX4: track 0.00 -> 48.1 mm, vias 0 -> 6
- net /SDA1: track 0.00 -> 47.8 mm, vias 0 -> 1
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- added copper zone on PWR, net /3V3
- added copper zone on PWR, net /5V_INT
- added copper zone on PWR, net /6V_EXT
- added copper zone on PWR, net /VBATT
- added copper zone on GND, net GND
- removed copper zone on L3, net /3V3
- removed copper zone on L2, net GND
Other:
- board size 95 x 50 mm -> 100 x 50 mm
- net class Default: clearance 0.19999 -> 0.0889; via_dia 0.6858 -> 0.508; via_drill 0.3302 -> 0.254
- net class PWR: clearance 0.19999 -> 0.2032; trace_width 0.7 -> 0.635; via_dia 0.6858 -> 0.508; via_drill 0.3302 -> 0.254
- rule trace_clearance: 0.19999 -> 0.0889
- rule trace_min: 0.2032 -> 0.0889
- rule via_min_drill: 0.3048 -> 0.2
- rule via_min_size: 0.6 -> 0.254
- board text added: "I2C"
- board text added: "SPI"
- board text added: "UART"
- board text removed: "Stackup: L1 (Front): Main components and routing L2: Ground L3: 3.3V L4 (Back): USB, SD, more components and routing"
